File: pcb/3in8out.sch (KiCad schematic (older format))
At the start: 24 parts

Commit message: rename Digits6.sch to 3in8out.sch.
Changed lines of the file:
@@
 	3400 1800 3550 1800
 Wire Wire Line
-	3850 1450 3850 1550
-Wire Wire Line
-	3850 1550 3850 1600
+	3850 1450 3850 1600
 Wire Wire Line
 	3100 2100 3000 2100
@@
 	3000 2100 3000 1800
 Wire Wire Line
-	2600 1800 3000 1800
-Wire Wire Line
-	3000 1800 3100 1800
+	2600 1800 3100 1800
 Connection ~ 3000 1800
 Wire Wire Line
-	3400 2100 3900 2100
-Wire Wire Line
-	3900 2100 4750 2100
-Wire Wire Line
-	3850 1550 4000 1550
-Wire Wire Line
-	4000 1550 4750 1550
+	3400 2100 4750 2100
+Wire Wire Line
+	3850 1550 4750 1550
 Connection ~ 3850 1550
 Wire Wire Line
@@
 	3100 2750 3200 2750
 Wire Wire Line
-	3500 1450 3500 2300
-Wire Wire Line
-	3500 2300 3500 2550
+	3500 1450 3500 2550
 Wire Wire Line
 	2800 3200 2700 3200
@@
 	2700 3200 2700 2750
 Wire Wire Line
-	2600 2750 2700 2750
-Wire Wire Line
-	2700 2750 2800 2750
+	2600 2750 2800 2750
 Connection ~ 2700 2750
 Wire Wire Line
 	3500 2950 3500 3050
 Wire Wire Line
-	3100 3200 4450 3200
-Wire Wire Line
-	4450 3200 4750 3200
-Wire Wire Line
-	3500 2300 4450 2300
-Wire Wire Line
-	4450 2300 4750 2300
+	3100 3200 4750 3200
+Wire Wire Line
+	3500 2300 4750 2300
 Connection ~ 3500 2300
 Wire Wire Line
@@
 Connection ~ 4450 3200
 Wire Wire Line
-	3400 3050 3500 3050
-Wire Wire Line
-	3500 3050 3850 3050
+	3400 3050 3850 3050
 $Comp
 L CSC388A Q?
@@
 	3100 4700 3200 4700
 Wire Wire Line
-	3100 4250 3500 4250
-Wire Wire Line
-	3500 4250 6700 4250
-Wire Wire Line
-	6700 4250 6800 4250
+	3100 4250 6800 4250
 Wire Wire Line
 	3500 4250 3500 4500
 Wire Wire Line
-	2600 3600 2700 3600
-Wire Wire Line
-	2700 3600 2800 3600
+	2600 3600 2800 3600
 Wire Wire Line
 	2700 3600 2700 4700
@@
 $EndComp
 Wire Wire Line
-	5950 1650 6650 1650
-Wire Wire Line
-	6650 1650 6850 1650
+	5950 1650 6850 1650
 Wire Wire Line
 	6800 4050 6650 4050
@@
 Connection ~ 6650 1650
 Wire Wire Line
-	5950 2200 6500 2200
-Wire Wire Line
-	6500 2200 6850 2200
-Wire Wire Line
-	5950 2750 6350 2750
-Wire Wire Line
-	6350 2750 6850 2750
-Wire Wire Line
-	5950 3300 6200 3300
-Wire Wire Line
-	6200 3300 6850 3300
+	5950 2200 6850 2200
+Wire Wire Line
+	5950 2750 6850 2750
+Wire Wire Line
+	5950 3300 6850 3300
 Wire Wire Line
 	6800 4600 6500 4600
@@
 Connection ~ 2700 3600
 Wire Wire Line
-	6750 1850 6750 2400
-Wire Wire Line
-	6750 2400 6750 2950
-Wire Wire Line
-	6750 2950 6750 3500
-Wire Wire Line
-	6750 3500 6750 3600
+	6750 1850 6750 3600
 Wire Wire Line
 	6750 2950 6850 2950
@@
 Connection ~ 6750 2400
 Wire Wire Line
-	6700 4250 6700 4800
-Wire Wire Line
-	6700 4800 6700 5350
-Wire Wire Line
-	6700 5350 6700 5900
+	6700 4250 6700 5900
 Wire Wire Line
 	6700 5900 6800 5900
@@
 TVCC
 Wire Wire Line
-	2600 1050 3500 1050
-Wire Wire Line
-	3500 1050 3850 1050
+	2600 1050 3850 1050
 Wire Wire Line
 	3850 1050 3850 1150

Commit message: annotate.
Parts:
- gave numbers to parts that had none: 15
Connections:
- net GND_T1: no longer U4.7 (GND_T1), U4.7 (GND_T1), U4.7 (GND_T1), U5.7 (GND_T1), U5.7 (GND_T1), U5.7 (GND_T1), U6.7 (GND_T1), U6.7 (GND_T1), U6.7 (GND_T1)
- net VCC_T1: no longer U4.14 (VCC_T1), U4.14 (VCC_T1), U4.14 (VCC_T1), U5.14 (VCC_T1), U5.14 (VCC_T1), U5.14 (VCC_T1), U6.14 (VCC_T1), U6.14 (VCC_T1), U6.14 (VCC_T1)
- net Y1: now also U6.6; no longer U6.3
- net Y2: now also U6.8; no longer U6.3
- net Y3: now also U6.11; no longer U6.3
- net Y5: now also U5.6; no longer U5.3
- net Y6: now also U5.8; no longer U5.3
- net Y7: now also U5.11; no longer U5.3
- net at Q8.2 (C), R31.1, U4.1: now also U4.9; no longer U4.1
- net at Q6.2 (C), R30.1, U4.2: now also U4.5; no longer U4.2
- net at Q7.2 (C), R26.1, U5.2: now also U5.10, U5.13, U5.5; no longer U5.2, U5.2, U5.2
- new net: R29.2, U4.13, U4.4
- new net: U4.6, U5.4, U6.4
- new net: R24.2, U4.10, U4.12
- new net: U4.8, U5.9, U6.9
- new net: U4.11, U6.12
- new net: R25.2, U6.10, U6.13, U6.2, U6.5
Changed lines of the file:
@@
 $EndDescr
 $Comp
-L 74HC00 U?
+L 74HC00 U4
 U 1 1 5A10DC2D
 P 5350 1650
-F 0 "U?" H 5350 1700 50  0000 C CNN
+F 0 "U4" H 5350 1700 50  0000 C CNN
 F 1 "74HC00" H 5350 1550 50  0000 C CNN
 F 2 "" H 5350 1650 50  0001 C CNN
@@
 $EndComp
 $Comp
-L 74HC00 U?
-U 1 1 5A10DC34
+L 74HC00 U4
+U 2 1 5A10DC34
 P 5350 2200
-F 0 "U?" H 5350 2250 50  0000 C CNN
+F 0 "U4" H 5350 2250 50  0000 C CNN
 F 1 "74HC00" H 5350 2100 50  0000 C CNN
 F 2 "" H 5350 2200 50  0001 C CNN
 F 3 "" H 5350 2200 50  0001 C CNN
-	1    5350 2200
-	1    0    0    -1
-$EndComp
-$Comp
-L 74HC00 U?
-U 1 1 5A10DC3B
+	2    5350 2200
+	1    0    0    -1
+$EndComp
+$Comp
+L 74HC00 U4
+U 3 1 5A10DC3B
 P 5350 2750
-F 0 "U?" H 5350 2800 50  0000 C CNN
+F 0 "U4" H 5350 2800 50  0000 C CNN
 F 1 "74HC00" H 5350 2650 50  0000 C CNN
 F 2 "" H 5350 2750 50  0001 C CNN
 F 3 "" H 5350 2750 50  0001 C CNN
-	1    5350 2750
-	1    0    0    -1
-$EndComp
-$Comp
-L 74HC00 U?
-U 1 1 5A10DC42
+	3    5350 2750
+	1    0    0    -1
+$EndComp
+$Comp
+L 74HC00 U4
+U 4 1 5A10DC42
 P 5350 3300
-F 0 "U?" H 5350 3350 50  0000 C CNN
+F 0 "U4" H 5350 3350 50  0000 C CNN
 F 1 "74HC00" H 5350 3200 50  0000 C CNN
 F 2 "" H 5350 3300 50  0001 C CNN
 F 3 "" H 5350 3300 50  0001 C CNN
-	1    5350 3300
-	1    0    0    -1
-$EndComp
-$Comp
-L 74HC00 U?
+	4    5350 3300
+	1    0    0    -1
+$EndComp
+$Comp
+L 74HC00 U6
 U 1 1 5A10DC49
 P 7450 1750
-F 0 "U?" H 7450 1800 50  0000 C CNN
+F 0 "U6" H 7450 1800 50  0000 C CNN
 F 1 "74HC00" H 7450 1650 50  0000 C CNN
 F 2 "" H 7450 1750 50  0001 C CNN
@@
 $EndComp
 $Comp
-L 74HC00 U?
-U 1 1 5A10DC50
+L 74HC00 U6
+U 2 1 5A10DC50
 P 7450 2300
-F 0 "U?" H 7450 2350 50  0000 C CNN
+F 0 "U6" H 7450 2350 50  0000 C CNN
 F 1 "74HC00" H 7450 2200 50  0000 C CNN
 F 2 "" H 7450 2300 50  0001 C CNN
 F 3 "" H 7450 2300 50  0001 C CNN
-	1    7450 2300
-	1    0    0    -1
-$EndComp
-$Comp
-L 74HC00 U?
-U 1 1 5A10DC57
+	2    7450 2300
+	1    0    0    -1
+$EndComp
+$Comp
+L 74HC00 U6
+U 3 1 5A10DC57
 P 7450 2850
-F 0 "U?" H 7450 2900 50  0000 C CNN
+F 0 "U6" H 7450 2900 50  0000 C CNN
 F 1 "74HC00" H 7450 2750 50  0000 C CNN
 F 2 "" H 7450 2850 50  0001 C CNN
 F 3 "" H 7450 2850 50  0001 C CNN
-	1    7450 2850
-	1    0    0    -1
-$EndComp
-$Comp
-L 74HC00 U?
-U 1 1 5A10DC5E
+	3    7450 2850
+	1    0    0    -1
+$EndComp
+$Comp
+L 74HC00 U6
+U 4 1 5A10DC5E
 P 7450 3400
-F 0 "U?" H 7450 3450 50  0000 C CNN
+F 0 "U6" H 7450 3450 50  0000 C CNN
 F 1 "74HC00" H 7450 3300 50  0000 C CNN
 F 2 "" H 7450 3400 50  0001 C CNN
 F 3 "" H 7450 3400 50  0001 C CNN
-	1    7450 3400
-	1    0    0    -1
-$EndComp
-$Comp
-L 74HC00 U?
+	4    7450 3400
+	1    0    0    -1
+$EndComp
+$Comp
+L 74HC00 U5
 U 1 1 5A10DC65
 P 7400 4150
-F 0 "U?" H 7400 4200 50  0000 C CNN
+F 0 "U5" H 7400 4200 50  0000 C CNN
 F 1 "74HC00" H 7400 4050 50  0000 C CNN
 F 2 "" H 7400 4150 50  0001 C CNN
@@
 $EndComp
 $Comp
-L 74HC00 U?
-U 1 1 5A10DC6C
+L 74HC00 U5
+U 2 1 5A10DC6C
 P 7400 4700
-F 0 "U?" H 7400 4750 50  0000 C CNN
+F 0 "U5" H 7400 4750 50  0000 C CNN
 F 1 "74HC00" H 7400 4600 50  0000 C CNN
 F 2 "" H 7400 4700 50  0001 C CNN
 F 3 "" H 7400 4700 50  0001 C CNN
-	1    7400 4700
-	1    0    0    -1
-$EndComp
-$Comp
-L 74HC00 U?
-U 1 1 5A10DC73
+	2    7400 4700
+	1    0    0    -1
+$EndComp
+$Comp
+L 74HC00 U5
+U 3 1 5A10DC73
 P 7400 5250
-F 0 "U?" H 7400 5300 50  0000 C CNN
+F 0 "U5" H 7400 5300 50  0000 C CNN
 F 1 "74HC00" H 7400 5150 50  0000 C CNN
 F 2 "" H 7400 5250 50  0001 C CNN
 F 3 "" H 7400 5250 50  0001 C CNN
-	1    7400 5250
-	1    0    0    -1
-$EndComp
-$Comp
-L 74HC00 U?
-U 1 1 5A10DC7A
+	3    7400 5250
+	1    0    0    -1
+$EndComp
+$Comp
+L 74HC00 U5
+U 4 1 5A10DC7A
 P 7400 5800
-F 0 "U?" H 7400 5850 50  0000 C CNN
+F 0 "U5" H 7400 5850 50  0000 C CNN
 F 1 "74HC00" H 7400 5700 50  0000 C CNN
 F 2 "" H 7400 5800 50  0001 C CNN
 F 3 "" H 7400 5800 50  0001 C CNN
-	1    7400 5800
-	1    0    0    -1
-$EndComp
-$Comp
-L CSC388A Q?
+	4    7400 5800
+	1    0    0    -1
+$EndComp
+$Comp
+L CSC388A Q8
 U 1 1 5A10DC81
 P 3750 1800
-F 0 "Q?" H 3700 1950 50  0000 L CNN
+F 0 "Q8" H 3700 1950 50  0000 L CNN
 F 1 "CSC388A" V 3950 1650 50  0000 L CNN
 F 2 "TO_SOT_Packages_THT:TO-92_Molded_Narrow" H 3950 1725 50  0001 L CIN
@@
 $EndComp
 $Comp
-L R R?
+L R R28
 U 1 1 5A10DC88
 P 3250 1800
-F 0 "R?" V 3330 1800 50  0000 C CNN
+F 0 "R28" V 3330 1800 50  0000 C CNN
 F 1 "10k" V 3250 1800 50  0000 C CNN
 F 2 "" V 3180 1800 50  0001 C CNN
@@
 $EndComp
 $Comp
-L R R?
+L R R31
 U 1 1 5A10DC8F
 P 3850 1300
-F 0 "R?" V 3930 1300 50  0000 C CNN
+F 0 "R31" V 3930 1300 50  0000 C CNN
 F 1 "2.2M" V 3850 1300 50  0000 C CNN
 F 2 "" V 3780 1300 50  0001 C CNN
@@
 $EndComp
 $Comp
-L R R?
+L R R29
 U 1 1 5A10DC96
 P 3250 2100
-F 0 "R?" V 3330 2100 50  0000 C CNN
+F 0 "R29" V 3330 2100 50  0000 C CNN
 F 1 "2.2M" V 3250 2100 50  0000 C CNN
 F 2 "" V 3180 2100 50  0001 C CNN
@@
 $EndComp
 $Comp
-L CSC388A Q?
+L CSC388A Q6
 U 1 1 5A10DC9D
 P 3400 2750
-F 0 "Q?" H 3350 2900 50  0000 L CNN
+F 0 "Q6" H 3350 2900 50  0000 L CNN
 F 1 "CSC388A" V 3600 2600 50  0000 L CNN
 F 2 "TO_SOT_Packages_THT:TO-92_Molded_Narrow" H 3600 2675 50  0001 L CIN
@@
 $EndComp
 $Comp
-L R R?
+L R R23
 U 1 1 5A10DCA4
 P 2950 2750
-F 0 "R?" V 3030 2750 50  0000 C CNN
+F 0 "R23" V 3030 2750 50  0000 C CNN
 F 1 "10k" V 2950 2750 50  0000 C CNN
 F 2 "" V 2880 2750 50  0001 C CNN
@@
 $EndComp
 $Comp
-L R R?
+L R R30
 U 1 1 5A10DCAB
 P 3500 1300
-F 0 "R?" V 3580 1300 50  0000 C CNN
+F 0 "R30" V 3580 1300 50  0000 C CNN
 F 1 "2.2M" V 3500 1300 50  0000 C CNN
 F 2 "" V 3430 1300 50  0001 C CNN
@@
 $EndComp
 $Comp
-L R R?
+L R R24
 U 1 1 5A10DCB2
 P 2950 3200
-F 0 "R?" V 3030 3200 50  0000 C CNN
+F 0 "R24" V 3030 3200 50  0000 C CNN
 F 1 "2.2M" V 2950 3200 50  0000 C CNN
 F 2 "" V 2880 3200 50  0001 C CNN
@@
 	3400 3050 3850 3050
 $Comp
-L CSC388A Q?
+L CSC388A Q7
 U 1 1 5A10DCE5
 P 3400 4700
-F 0 "Q?" H 3350 4850 50  0000 L CNN
+F 0 "Q7" H 3350 4850 50  0000 L CNN
 F 1 "CSC388A" V 3600 4550 50  0000 L CNN
 F 2 "TO_SOT_Packages_THT:TO-92_Molded_Narrow" H 3600 4625 50  0001 L CIN
@@
 $EndComp
 $Comp
-L R R?
+L R R27
 U 1 1 5A10DCEC
 P 2950 4700
-F 0 "R?" V 3030 4700 50  0000 C CNN
+F 0 "R27" V 3030 4700 50  0000 C CNN
 F 1 "10k" V 2950 4700 50  0000 C CNN
 F 2 "" V 2880 4700 50  0001 C CNN
@@
 $EndComp
 $Comp
-L R R?
+L R R25
 U 1 1 5A10DCF3
 P 2950 3600
-F 0 "R?" V 3030 3600 50  0000 C CNN
+F 0 "R25" V 3030 3600 50  0000 C CNN
 F 1 "2.2M" V 2950 3600 50  0000 C CNN
 F 2 "" V 2880 3600 50  0001 C CNN
@@
 	6750 3600 3100 3600
 $Comp
-L R R?
+L R R26
 U 1 1 5A10DD03
 P 2950 4250
-F 0 "R?" V 3030 4250 50  0000 C CNN
+F 0 "R26" V 3030 4250 50  0000 C CNN
 F 1 "2.2M" V 2950 4250 50  0000 C CNN
 F 2 "" V 2880 4250 50  0001 C CNN

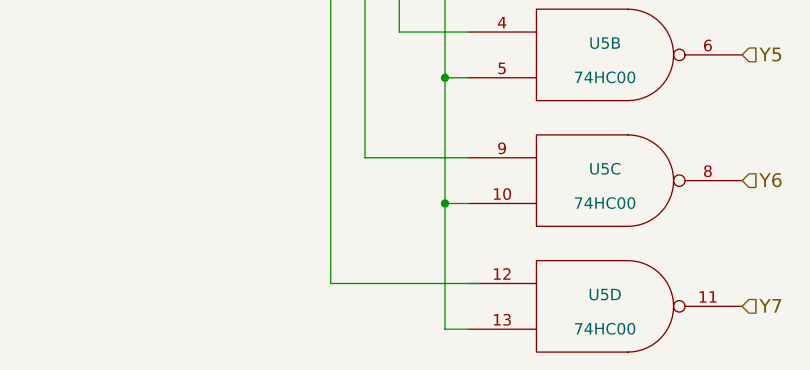
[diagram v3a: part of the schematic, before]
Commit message: 細々した配線誤りを修正。 fixed tiny mistake.
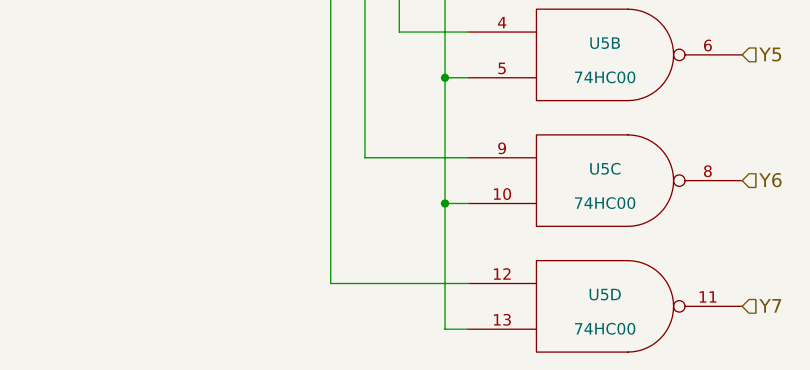
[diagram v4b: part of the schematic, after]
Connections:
- net at U4.11, U6.12: now also U5.12
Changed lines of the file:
@@
 	6800 5150 6350 5150
-Wire Wire Line
-	6850 5700 6200 5700
 Wire Wire Line
 	6200 5700 6200 3300
@@
 TGND
 Connection ~ 3500 3050
+Wire Wire Line
+	6800 5700 6200 5700
 $EndSCHEMATC

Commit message: 3in8out 回路に CvPcb で部品を割り当てた。
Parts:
- R23, R24, R25, R26, R27, R28, R29, R30, R31: footprint (none) -> Resistors_THT:R_Axial_DIN0207_L6.3mm_D2.5mm_P7.62mm_Horizontal
- U4, U5, U6: footprint (none) -> Housings_DIP:DIP-14_W7.62mm
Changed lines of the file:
@@
 F 0 "U4" H 5350 1700 50  0000 C CNN
 F 1 "74HC00" H 5350 1550 50  0000 C CNN
-F 2 "" H 5350 1650 50  0001 C CNN
+F 2 "Housings_DIP:DIP-14_W7.62mm" H 5350 1650 50  0001 C CNN
 F 3 "" H 5350 1650 50  0001 C CNN
 	1    5350 1650
@@
 F 0 "U4" H 5350 2250 50  0000 C CNN
 F 1 "74HC00" H 5350 2100 50  0000 C CNN
-F 2 "" H 5350 2200 50  0001 C CNN
+F 2 "Housings_DIP:DIP-14_W7.62mm" H 5350 2200 50  0001 C CNN
 F 3 "" H 5350 2200 50  0001 C CNN
 	2    5350 2200
@@
 F 0 "U4" H 5350 2800 50  0000 C CNN
 F 1 "74HC00" H 5350 2650 50  0000 C CNN
-F 2 "" H 5350 2750 50  0001 C CNN
+F 2 "Housings_DIP:DIP-14_W7.62mm" H 5350 2750 50  0001 C CNN
 F 3 "" H 5350 2750 50  0001 C CNN
 	3    5350 2750
@@
 F 0 "U4" H 5350 3350 50  0000 C CNN
 F 1 "74HC00" H 5350 3200 50  0000 C CNN
-F 2 "" H 5350 3300 50  0001 C CNN
+F 2 "Housings_DIP:DIP-14_W7.62mm" H 5350 3300 50  0001 C CNN
 F 3 "" H 5350 3300 50  0001 C CNN
 	4    5350 3300
@@
 F 0 "U6" H 7450 1800 50  0000 C CNN
 F 1 "74HC00" H 7450 1650 50  0000 C CNN
-F 2 "" H 7450 1750 50  0001 C CNN
+F 2 "Housings_DIP:DIP-14_W7.62mm" H 7450 1750 50  0001 C CNN
 F 3 "" H 7450 1750 50  0001 C CNN
 	1    7450 1750
@@
 F 0 "U6" H 7450 2350 50  0000 C CNN
 F 1 "74HC00" H 7450 2200 50  0000 C CNN
-F 2 "" H 7450 2300 50  0001 C CNN
+F 2 "Housings_DIP:DIP-14_W7.62mm" H 7450 2300 50  0001 C CNN
 F 3 "" H 7450 2300 50  0001 C CNN
 	2    7450 2300
@@
 F 0 "U6" H 7450 2900 50  0000 C CNN
 F 1 "74HC00" H 7450 2750 50  0000 C CNN
-F 2 "" H 7450 2850 50  0001 C CNN
+F 2 "Housings_DIP:DIP-14_W7.62mm" H 7450 2850 50  0001 C CNN
 F 3 "" H 7450 2850 50  0001 C CNN
 	3    7450 2850
@@
 F 0 "U6" H 7450 3450 50  0000 C CNN
 F 1 "74HC00" H 7450 3300 50  0000 C CNN
-F 2 "" H 7450 3400 50  0001 C CNN
+F 2 "Housings_DIP:DIP-14_W7.62mm" H 7450 3400 50  0001 C CNN
 F 3 "" H 7450 3400 50  0001 C CNN
 	4    7450 3400
@@
 F 0 "U5" H 7400 4200 50  0000 C CNN
 F 1 "74HC00" H 7400 4050 50  0000 C CNN
-F 2 "" H 7400 4150 50  0001 C CNN
+F 2 "Housings_DIP:DIP-14_W7.62mm" H 7400 4150 50  0001 C CNN
 F 3 "" H 7400 4150 50  0001 C CNN
 	1    7400 4150
@@
 F 0 "U5" H 7400 4750 50  0000 C CNN
 F 1 "74HC00" H 7400 4600 50  0000 C CNN
-F 2 "" H 7400 4700 50  0001 C CNN
+F 2 "Housings_DIP:DIP-14_W7.62mm" H 7400 4700 50  0001 C CNN
 F 3 "" H 7400 4700 50  0001 C CNN
 	2    7400 4700
@@
 F 0 "U5" H 7400 5300 50  0000 C CNN
 F 1 "74HC00" H 7400 5150 50  0000 C CNN
-F 2 "" H 7400 5250 50  0001 C CNN
+F 2 "Housings_DIP:DIP-14_W7.62mm" H 7400 5250 50  0001 C CNN
 F 3 "" H 7400 5250 50  0001 C CNN
 	3    7400 5250
@@
 F 0 "U5" H 7400 5850 50  0000 C CNN
 F 1 "74HC00" H 7400 5700 50  0000 C CNN
-F 2 "" H 7400 5800 50  0001 C CNN
+F 2 "Housings_DIP:DIP-14_W7.62mm" H 7400 5800 50  0001 C CNN
 F 3 "" H 7400 5800 50  0001 C CNN
 	4    7400 5800
@@
 F 0 "R28" V 3330 1800 50  0000 C CNN
 F 1 "10k" V 3250 1800 50  0000 C CNN
-F 2 "" V 3180 1800 50  0001 C CNN
+F 2 "Resistors_THT:R_Axial_DIN0207_L6.3mm_D2.5mm_P7.62mm_Horizontal" V 3180 1800 50  0001 C CNN
 F 3 "" H 3250 1800 50  0001 C CNN
 	1    3250 1800
@@
 F 0 "R31" V 3930 1300 50  0000 C CNN
 F 1 "2.2M" V 3850 1300 50  0000 C CNN
-F 2 "" V 3780 1300 50  0001 C CNN
+F 2 "Resistors_THT:R_Axial_DIN0207_L6.3mm_D2.5mm_P7.62mm_Horizontal" V 3780 1300 50  0001 C CNN
 F 3 "" H 3850 1300 50  0001 C CNN
 	1    3850 1300
@@
 F 0 "R29" V 3330 2100 50  0000 C CNN
 F 1 "2.2M" V 3250 2100 50  0000 C CNN
-F 2 "" V 3180 2100 50  0001 C CNN
+F 2 "Resistors_THT:R_Axial_DIN0207_L6.3mm_D2.5mm_P7.62mm_Horizontal" V 3180 2100 50  0001 C CNN
 F 3 "" H 3250 2100 50  0001 C CNN
 	1    3250 2100
@@
 F 0 "R23" V 3030 2750 50  0000 C CNN
 F 1 "10k" V 2950 2750 50  0000 C CNN
-F 2 "" V 2880 2750 50  0001 C CNN
+F 2 "Resistors_THT:R_Axial_DIN0207_L6.3mm_D2.5mm_P7.62mm_Horizontal" V 2880 2750 50  0001 C CNN
 F 3 "" H 2950 2750 50  0001 C CNN
 	1    2950 2750
@@
 F 0 "R30" V 3580 1300 50  0000 C CNN
 F 1 "2.2M" V 3500 1300 50  0000 C CNN
-F 2 "" V 3430 1300 50  0001 C CNN
+F 2 "Resistors_THT:R_Axial_DIN0207_L6.3mm_D2.5mm_P7.62mm_Horizontal" V 3430 1300 50  0001 C CNN
 F 3 "" H 3500 1300 50  0001 C CNN
 	1    3500 1300
@@
 F 0 "R24" V 3030 3200 50  0000 C CNN
 F 1 "2.2M" V 2950 3200 50  0000 C CNN
-F 2 "" V 2880 3200 50  0001 C CNN
+F 2 "Resistors_THT:R_Axial_DIN0207_L6.3mm_D2.5mm_P7.62mm_Horizontal" V 2880 3200 50  0001 C CNN
 F 3 "" H 2950 3200 50  0001 C CNN
 	1    2950 3200
@@
 F 0 "R27" V 3030 4700 50  0000 C CNN
 F 1 "10k" V 2950 4700 50  0000 C CNN
-F 2 "" V 2880 4700 50  0001 C CNN
+F 2 "Resistors_THT:R_Axial_DIN0207_L6.3mm_D2.5mm_P7.62mm_Horizontal" V 2880 4700 50  0001 C CNN
 F 3 "" H 2950 4700 50  0001 C CNN
 	1    2950 4700
@@
 F 0 "R25" V 3030 3600 50  0000 C CNN
 F 1 "2.2M" V 2950 3600 50  0000 C CNN
-F 2 "" V 2880 3600 50  0001 C CNN
+F 2 "Resistors_THT:R_Axial_DIN0207_L6.3mm_D2.5mm_P7.62mm_Horizontal" V 2880 3600 50  0001 C CNN
 F 3 "" H 2950 3600 50  0001 C CNN
 	1    2950 3600
@@
 F 0 "R26" V 3030 4250 50  0000 C CNN
 F 1 "2.2M" V 2950 4250 50  0000 C CNN
-F 2 "" V 2880 4250 50  0001 C CNN
+F 2 "Resistors_THT:R_Axial_DIN0207_L6.3mm_D2.5mm_P7.62mm_Horizontal" V 2880 4250 50  0001 C CNN
 F 3 "" H 2950 4250 50  0001 C CNN
 	1    2950 4250
